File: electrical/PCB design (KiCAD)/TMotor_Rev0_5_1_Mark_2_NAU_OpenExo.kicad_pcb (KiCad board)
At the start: 2 copper layers, 89.3 x 79.4 mm, 88 parts, among them J1 Conn_01x07_Pin, J2 Conn_01x04_Pin, J3 Conn_01x02_Pin, J4 Conn_01x02_Pin, J5 Conn_01x02_Pin, J6 Conn_01x02_Pin, J7 Conn_01x03_Pin, U1 TXU0104PWR, U10 DEV-16771, U2 TXU0304-Q1, U3 INA125U, U4 INA125U, U5 SN65HVD230DR, U6 INA125U, U7 INA125U

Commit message: update
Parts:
- removed pinout_origin: Pinout Origin: Place at image top left., Pinout tentative layout:Origin
- removed pinout_pinlabel (x3): GND {{pwr}}, Pinout tentative layout:PinLabel
- removed pinout_pinlabel: RST {{nano}}, Pinout tentative layout:PinLabel
- removed pinout_pinlabel: GND {{teensy}} {{gpio}}, Pinout tentative layout:PinLabel
- removed pinout_pinlabel: SCL {{i2c}} {{teensy}} {{nano}}, Pinout tentative layout:PinLabel
- removed pinout_pinlabel: SDA {{i2c}} {{teensy}} {{nano}}, Pinout tentative layout:PinLabel
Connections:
- net /CAN and peripherals/CAN_N renamed /CAN and peripherals./CAN_N
- net /CAN and peripherals/CAN_P renamed /CAN and peripherals./CAN_P
- net /CAN and peripherals/L7_VIN renamed /CAN and peripherals./L7_VIN
- net /CAN and peripherals/VBATT renamed /CAN and peripherals./VBATT

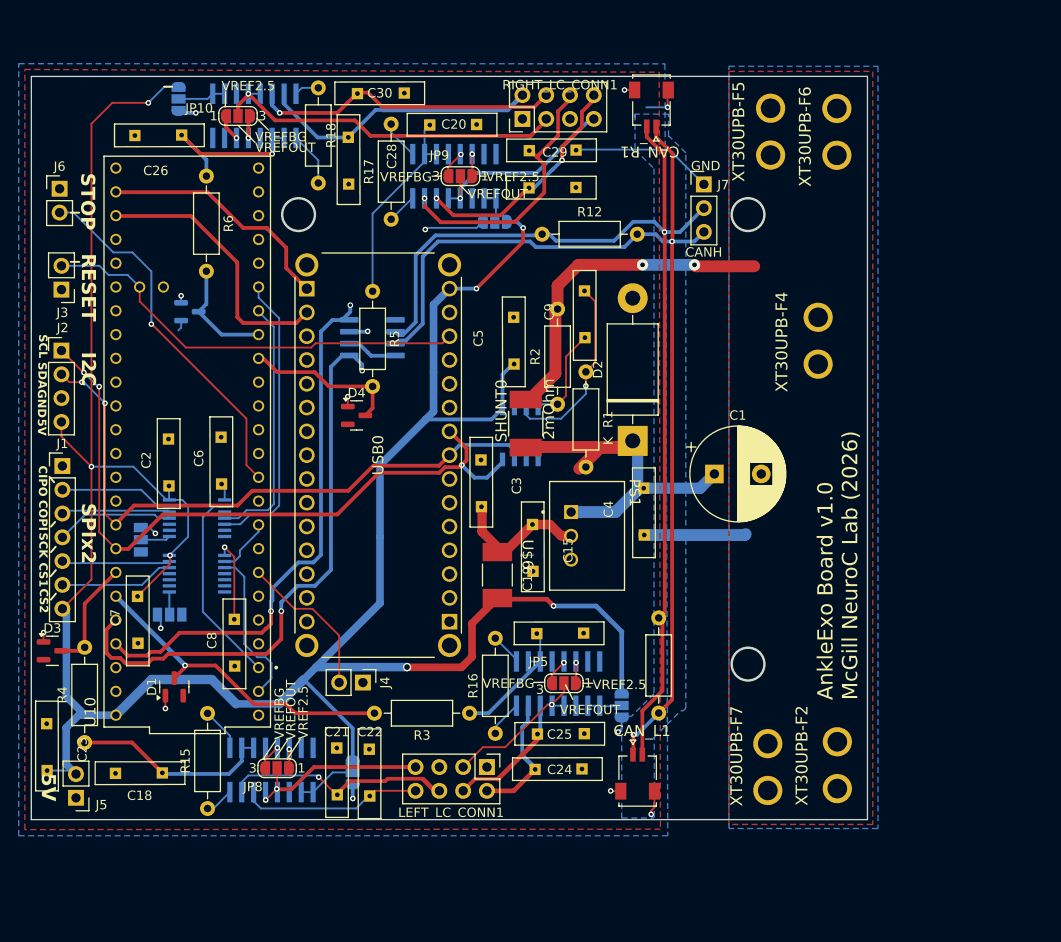
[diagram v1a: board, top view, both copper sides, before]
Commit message: 26/06 schematics updates
see the changelog on the documentation /electrical/pcb
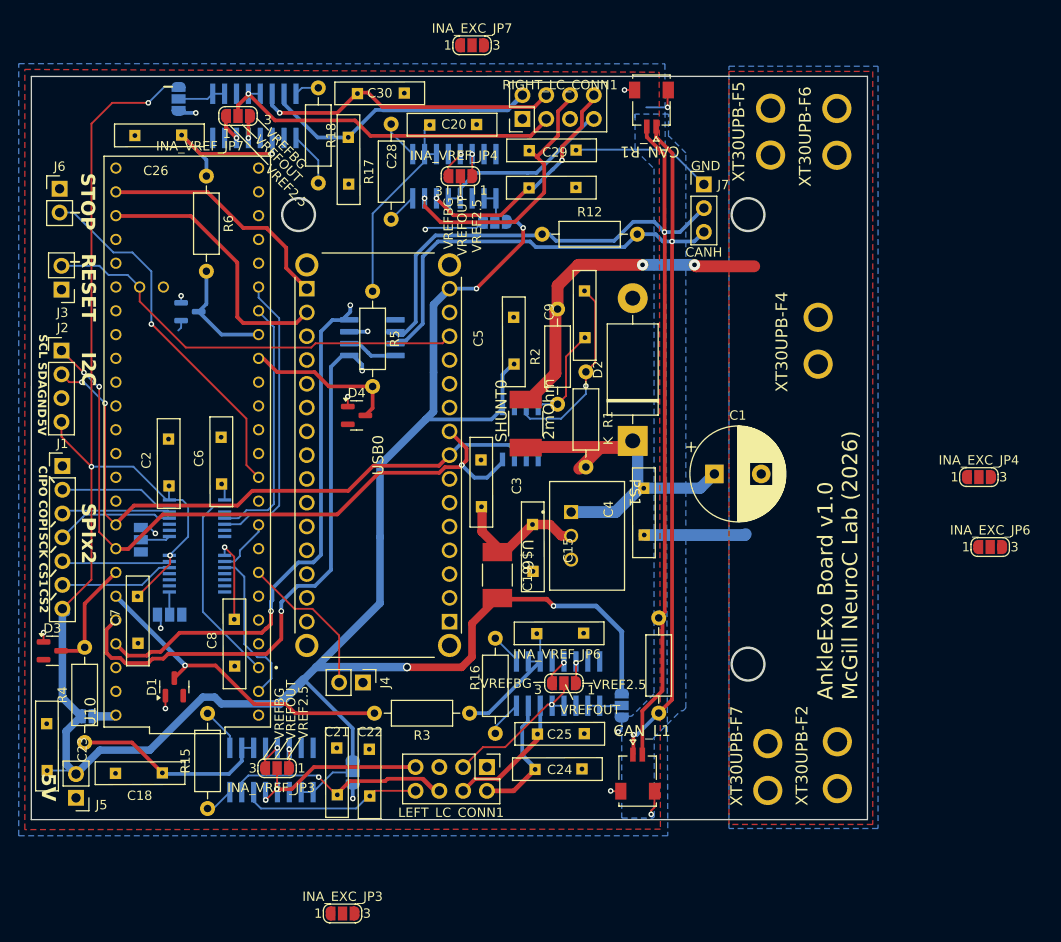
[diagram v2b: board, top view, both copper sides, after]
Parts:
- added INA_EXC_JP3: SolderJumper_3_Open, Jumper:SolderJumper-3_P1.3mm_Open_RoundedPad1.0x1.5mm_NumberLabels, F.Cu at (136.9, 154.7)
- added INA_EXC_JP4: SolderJumper_3_Open, Jumper:SolderJumper-3_P1.3mm_Open_RoundedPad1.0x1.5mm_NumberLabels, F.Cu at (204.8, 108.1)
- added INA_EXC_JP6: SolderJumper_3_Open, Jumper:SolderJumper-3_P1.3mm_Open_RoundedPad1.0x1.5mm_NumberLabels, F.Cu at (206.1, 115.6)
- added INA_EXC_JP7: SolderJumper_3_Open, Jumper:SolderJumper-3_P1.3mm_Open_RoundedPad1.0x1.5mm_NumberLabels, F.Cu at (150.7, 62.0)
- added TeensyPowerJP1: SolderJumper_2_Open, Jumper:SolderJumper-2_P1.3mm_Open_RoundedPad1.0x1.5mm, B.Cu at (109.6, 133.7)
- renumbered JP6 to CSVoltageShifterOEJP1, JP2 to INA_PWR_JP3, JP3 to INA_PWR_JP4, JP1 to INA_PWR_JP6, JP4 to INA_PWR_JP7, JP8 to INA_VREF_JP3, JP9 to INA_VREF_JP4, JP5 to INA_VREF_JP6, JP10 to INA_VREF_JP7, JP7 to SPIVoltageShifterOEJP1
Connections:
- INA_VREF_JP3 pad 2: /Load cells/Left LC  Amplifier 1/Vexcitation+ -> Net-(INA_EXC_JP3-B)
- INA_VREF_JP4 pad 2: /Load cells/Right LC  Amplifier 2/Vexcitation+ -> Net-(INA_EXC_JP4-B)
- INA_VREF_JP6 pad 2: /Load cells/Left LC Amplifier 2/Vexcitation+ -> Net-(INA_EXC_JP6-B)
- INA_VREF_JP7 pad 2: /Load cells/Right LC Amplifier 1/Vexcitation+ -> Net-(INA_EXC_JP7-B)
- U10 pad VIN: +5V -> Net-(TeensyPowerJP1-B)
- U3 pad 4: /Load cells/Left LC  Amplifier 1/Vexcitation+ -> Net-(INA_EXC_JP3-B)
- U3 pad 5: /Load cells/Left LC  Amplifier 1/Vexcitation+ -> Net-(INA_EXC_JP3-B)
- U4 pad 4: /Load cells/Right LC  Amplifier 2/Vexcitation+ -> Net-(INA_EXC_JP4-B)
- U4 pad 5: /Load cells/Right LC  Amplifier 2/Vexcitation+ -> Net-(INA_EXC_JP4-B)
- U6 pad 4: /Load cells/Left LC Amplifier 2/Vexcitation+ -> Net-(INA_EXC_JP6-B)
- U6 pad 5: /Load cells/Left LC Amplifier 2/Vexcitation+ -> Net-(INA_EXC_JP6-B)
- U7 pad 4: /Load cells/Right LC Amplifier 1/Vexcitation+ -> Net-(INA_EXC_JP7-B)
- U7 pad 5: /Load cells/Right LC Amplifier 1/Vexcitation+ -> Net-(INA_EXC_JP7-B)
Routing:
- net Net-(TeensyPowerJP1-B): track 0.00 -> 2.47 mm
- net +5V: track 279.8 -> 281.7 mm

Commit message: Updated KiCAD for next iteration (some minor fixes) ; functional Servo controller and MIT is working over serial
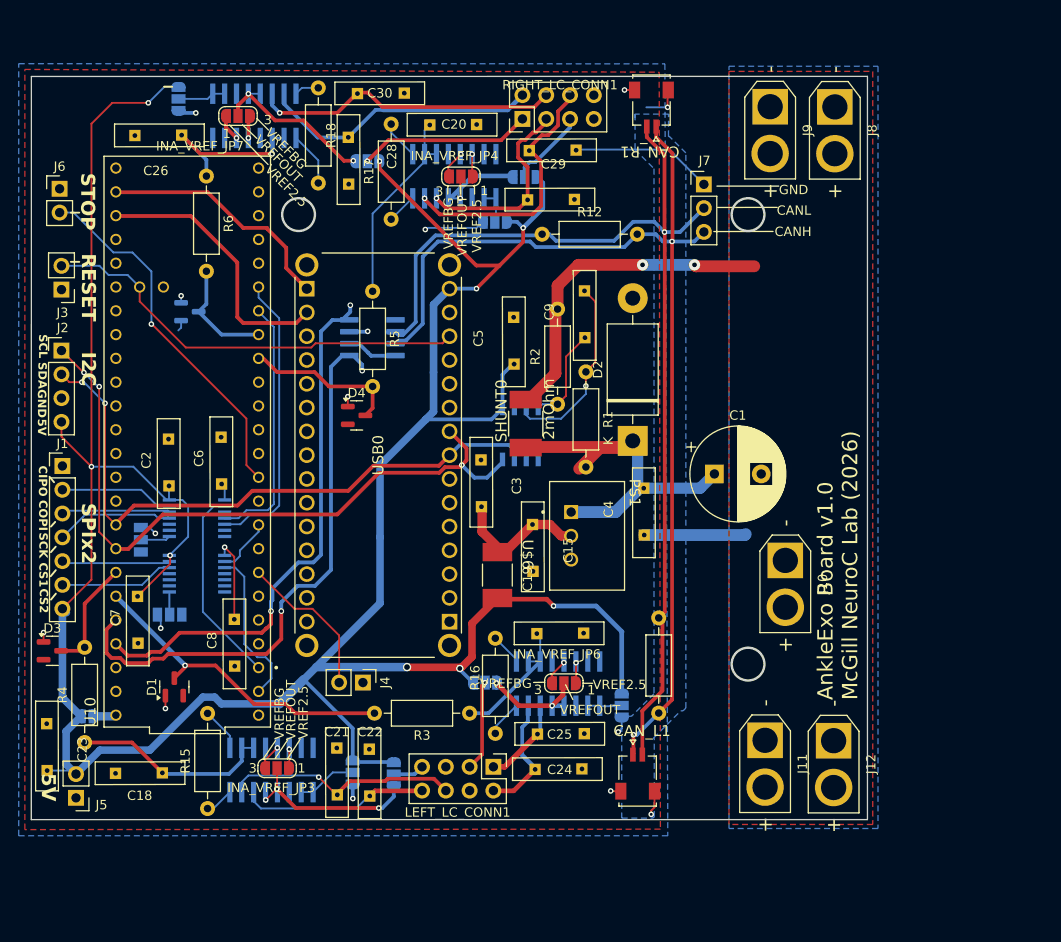
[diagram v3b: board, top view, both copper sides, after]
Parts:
- removed XT30UPB-F2, XT30UPB-F4, XT30UPB-F5, XT30UPB-F6, XT30UPB-F7: L_0, TMotor_Rev0_5_1_Mark_2_NAU_OpenExo:XT30UPB-F
- added J10: XT30PW-F, XT30PW-F:AMASS_XT30U-F_1x02_P5.0mm_Vertical, F.Cu at (184.2, 117.0)
- added J11: XT30PW-F, XT30PW-F:AMASS_XT30U-F_1x02_P5.0mm_Vertical, F.Cu at (182.0, 136.2)
- added J12: XT30PW-F, XT30PW-F:AMASS_XT30U-F_1x02_P5.0mm_Vertical, F.Cu at (189.3, 136.3)
- added J8: XT30PW-F, XT30PW-F:AMASS_XT30U-F_1x02_P5.0mm_Vertical, F.Cu at (189.5, 68.6)
- added J9: XT30PW-F, XT30PW-F:AMASS_XT30U-F_1x02_P5.0mm_Vertical, F.Cu at (182.6, 68.6)
- INA_EXC_JP3, INA_EXC_JP4, INA_EXC_JP6, INA_EXC_JP7: moved to B.Cu
- moved INA_EXC_JP4 58.1 mm to (156.3, 76.1), turned to 180 degrees
- moved INA_EXC_JP6 55.8 mm to (152.1, 130.1)
- moved INA_EXC_JP7 16.7 mm to (139.5, 74.4), turned to 180 degrees
- moved INA_EXC_JP3 15.8 mm to (142.4, 139.8), turned to -90 degrees
- moved C29 1.28 mm to (156.9, 78.5)
- moved LEFT_LC_CONN1 0.70 mm to (153.0, 139.1)
- moved INA_VREF_JP4 0.07 mm to (149.5, 76.0)
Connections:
- LEFT_LC_CONN1 pad 1: GND -> /Load cells/Left LC Amplifier 2/Vbridge+
- LEFT_LC_CONN1 pad 4: /Load cells/Left LC Amplifier 2/Vbridge+ -> GND
- RIGHT_LC_CONN1 pad 1: GND -> /Load cells/Right LC Amplifier 1/Vexcitation+
- RIGHT_LC_CONN1 pad 3: /Load cells/Right LC Amplifier 1/Vexcitation+ -> /Load cells/Right LC  Amplifier 2/Vbridge+
- RIGHT_LC_CONN1 pad 5: GND -> /Load cells/Right LC  Amplifier 2/Vexcitation+
- RIGHT_LC_CONN1 pad 7: /Load cells/Right LC  Amplifier 2/Vexcitation+ -> GND
- RIGHT_LC_CONN1 pad 8: /Load cells/Right LC  Amplifier 2/Vbridge+ -> GND
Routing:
- net +5V: track 281.7 -> 312.8 mm, vias 7 -> 9
- net /Load cells/Right LC Amplifier 1/Vexcitation+: track 38.6 -> 18.4 mm
- net Net-(INA_EXC_JP3-B): track 0.00 -> 18.9 mm, vias 0 -> 3
- net Net-(INA_EXC_JP7-B): track 0.00 -> 18.3 mm, vias 0 -> 2
- net /Load cells/Left LC  Amplifier 1/Vexcitation+: track 19.7 -> 3.35 mm, vias 2 -> 0
- net /Load cells/Right LC  Amplifier 2/Vexcitation+: track 22.1 -> 8.56 mm, vias 1 -> 0
- net Net-(INA_EXC_JP4-B): track 0.00 -> 12.6 mm, vias 0 -> 1
- net Net-(INA_EXC_JP6-B): track 0.00 -> 11.2 mm, vias 0 -> 2
- net /Load cells/Left LC Amplifier 2/Vexcitation+: track 16.4 -> 9.71 mm
- net /Load cells/Left LC Amplifier 2/Vbridge+: track 14.0 -> 9.90 mm
- net /Load cells/Right LC  Amplifier 2/Vbridge+: track 25.0 -> 21.4 mm, vias 2 -> 1
- net GND: track 45.1 -> 46.4 mm
- net /Load cells/Right LC  Amplifier 2/Vbridge-: track 28.9 -> 28.2 mm
- net /Load cells/Left LC  Amplifier 1/Vbridge+: track 20.8 -> 21.5 mm
- net /Load cells/Left LC  Amplifier 1/Vbridge-: track 25.5 -> 26.2 mm
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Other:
- board text added: "INARef"
